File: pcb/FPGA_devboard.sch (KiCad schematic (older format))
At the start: 2 parts, among them X3 AC7020, X4 Conn_02x05_Odd_Even

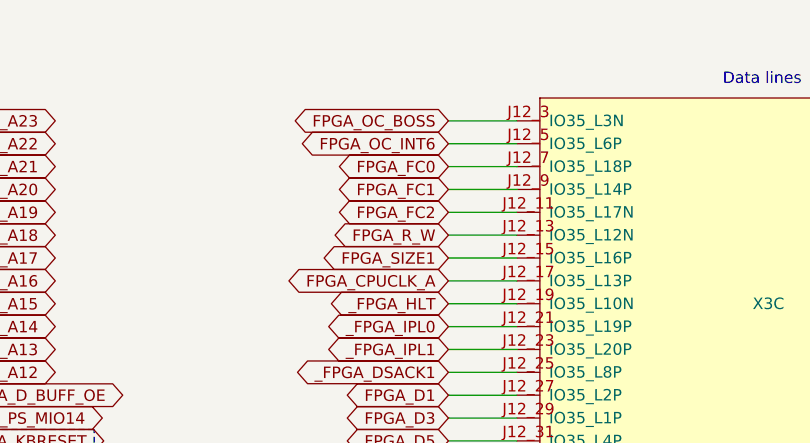
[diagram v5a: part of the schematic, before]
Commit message: remind myself to connect CPUCLK to clock-capable pin in the future board revisions
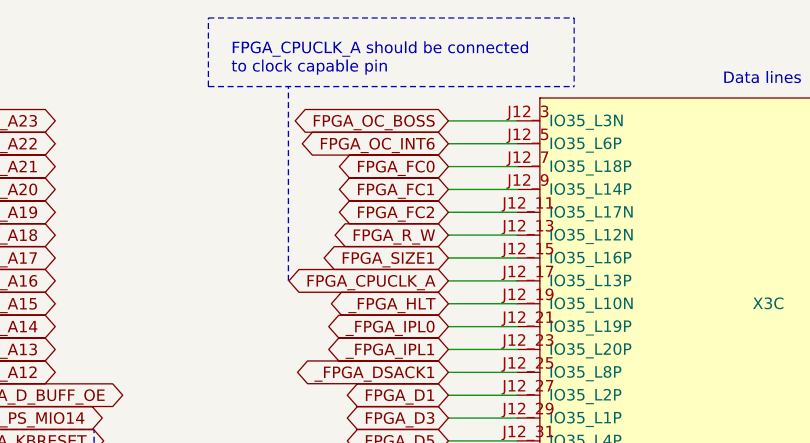
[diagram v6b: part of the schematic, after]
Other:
- note added: "FPGA_CPUCLK_A should be connected \nto clock capable pin"
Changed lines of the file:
@@
 Text GLabel 9600 2700 2    50   BiDi ~ 0
 _FPGA_DSACK0
+Text Notes 5850 1400 0    50   ~ 0
+FPGA_CPUCLK_A should be connected \nto clock capable pin
+Wire Notes Line
+	6100 2300 6100 1450
+Wire Notes Line
+	5750 1450 5750 1150
+Wire Notes Line
+	5750 1150 7350 1150
+Wire Notes Line
+	5750 1450 7350 1450
+Wire Notes Line
+	7350 1150 7350 1450
 $EndSCHEMATC
